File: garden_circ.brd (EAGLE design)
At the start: 89.8 x 83.8 mm, 39 parts, among them IC1 MEGA8-P, IC2 74HC595N, IC3 74HC595N, IC4 7805TV, J1 POWER_JACKSLT

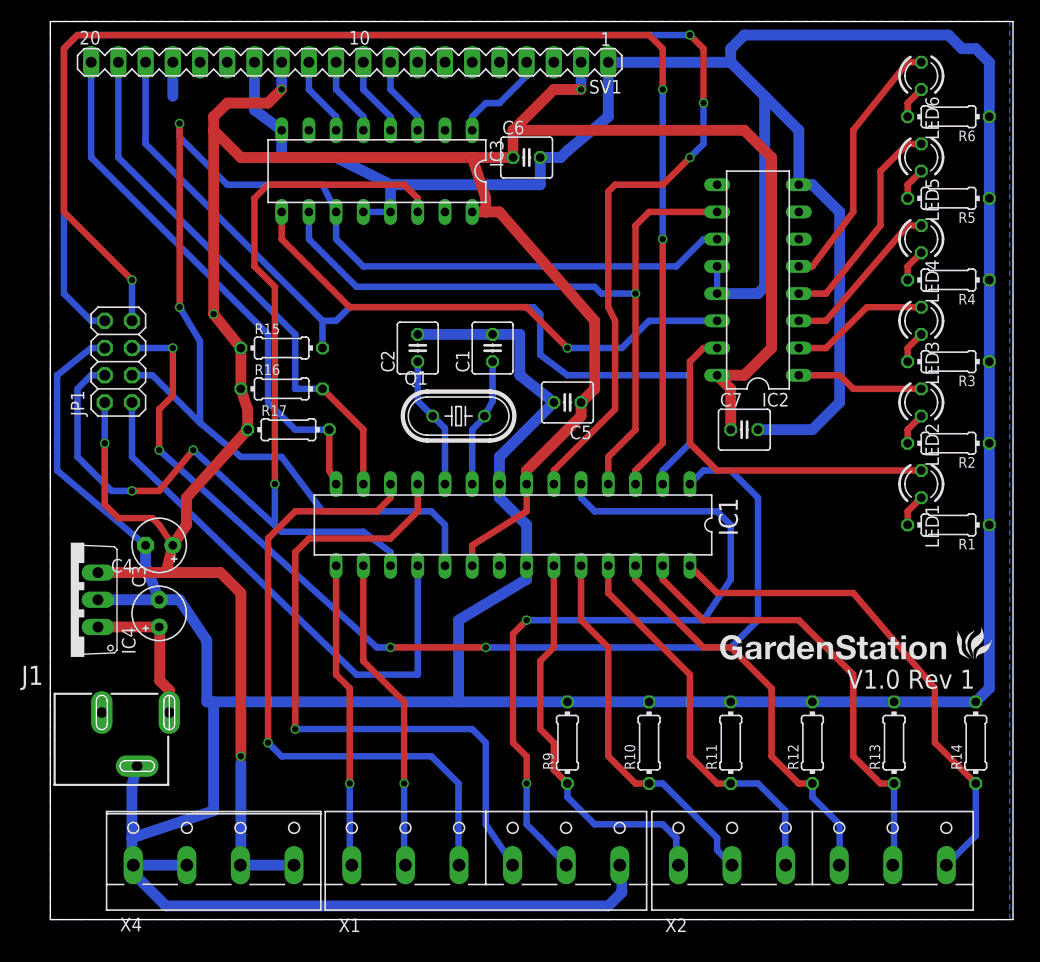
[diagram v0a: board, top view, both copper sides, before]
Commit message: Fixed shift register wiring
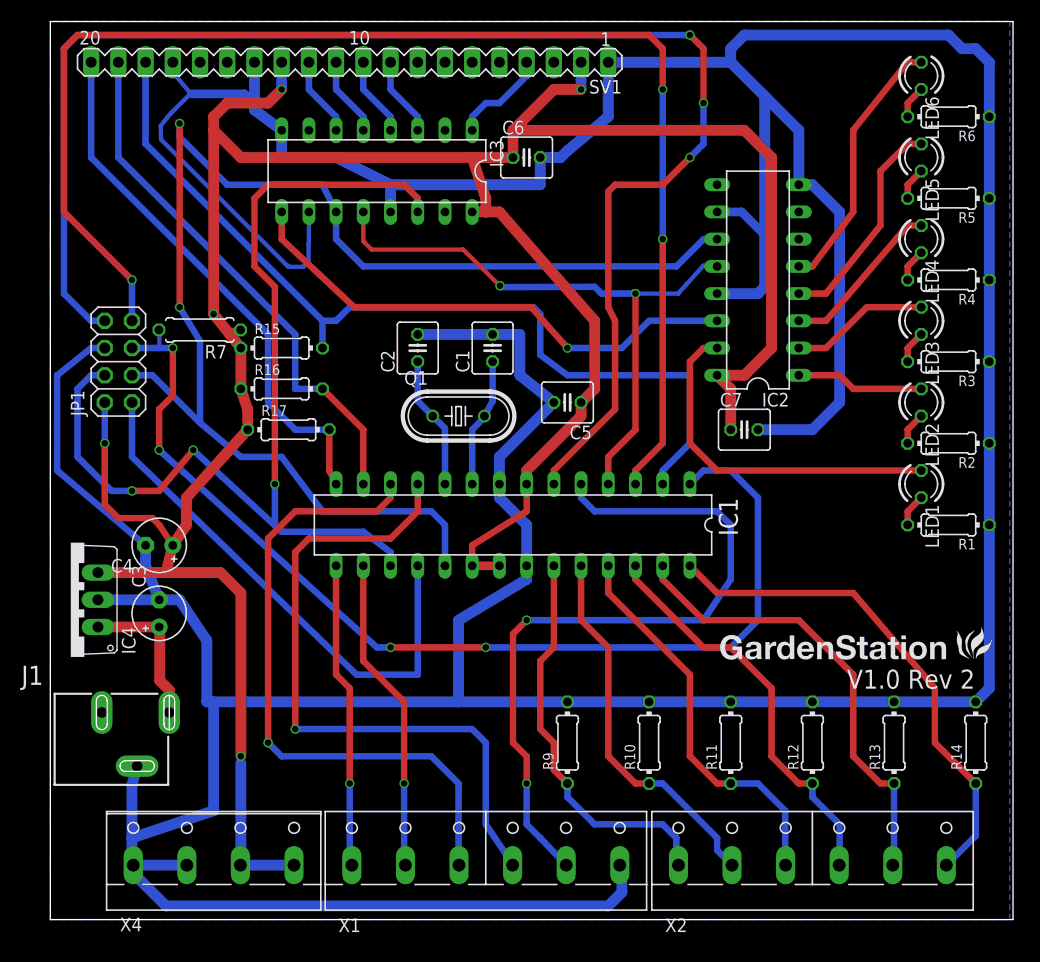
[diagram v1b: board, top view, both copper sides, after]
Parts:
- added R7: 10K, resistor:0207/7
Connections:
- removed net N$38: IC1.4, IC2.10, IC3.10
- new net N$52: IC1.4, IC2.12, IC3.12
- net GND: now also IC2.10, IC3.10; no longer IC2.12, IC3.12
- net N$10: now also R7.2
- net VCC: now also IC1.21, R7.1
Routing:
- net N$38: track 68.5 -> 0.00 mm
- net N$52: track 0.00 -> 58.2 mm, vias 0 -> 1
- net GND: track 483.2 -> 519.1 mm
- net VCC: track 264.7 -> 268.6 mm
- net N$10: track 97.3 -> 99.0 mm
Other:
- board text added: "V1.0 Rev 2"
- board text removed: "V1.0 Rev 1"

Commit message: Added code an SMD board
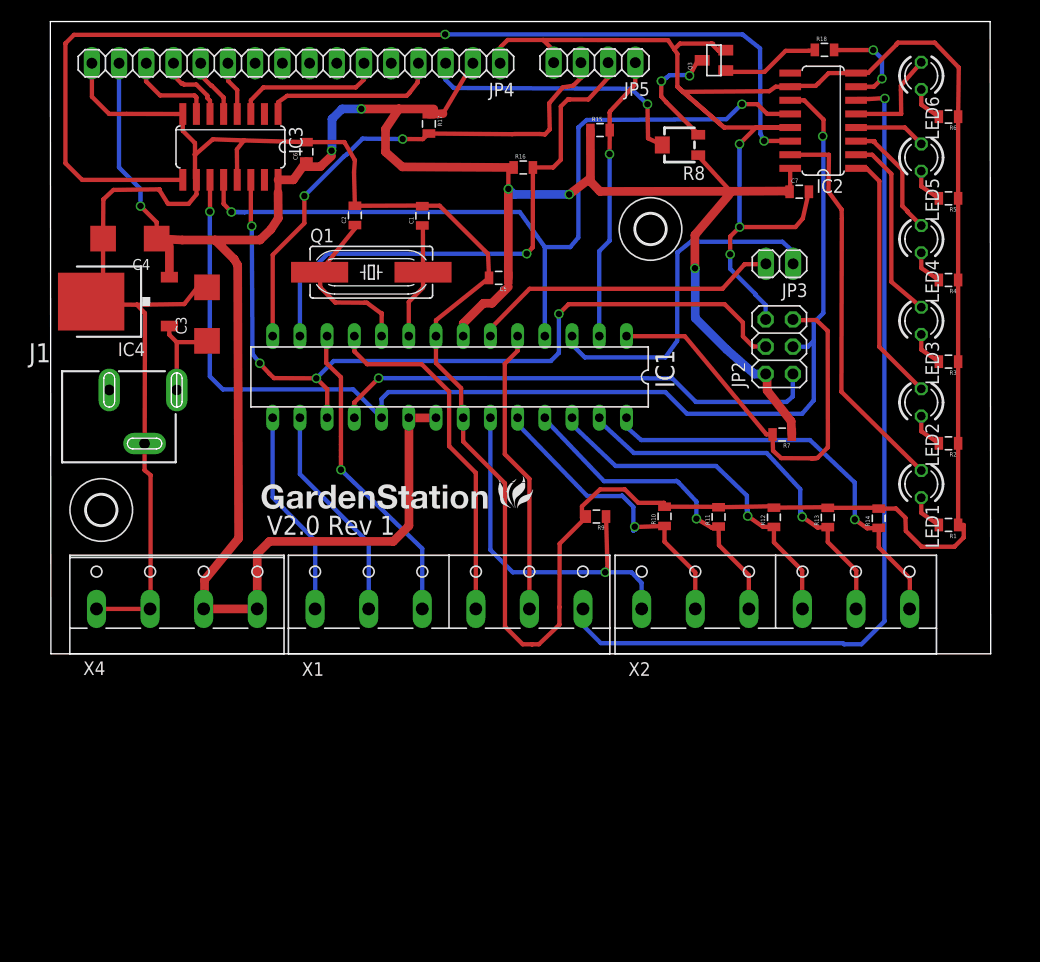
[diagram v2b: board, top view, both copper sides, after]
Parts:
- removed JP1: (no value), pinhead:2X04
- removed SV1: (no value), con-lstb:MA20-1
- added H1, H2: MOUNT-HOLE2.8, holes:2,8
- added JP2: (no value), pinhead:2X03
- added JP3: (no value), pinhead:1X02
- added JP4: (no value), pinhead:1X16
- added JP5: (no value), pinhead:1X04
- added Q3: MOSFET-NCHANNELBSS123LT1G, SparkFun-DiscreteSemi:SOT23
- added R18: (no value), SparkFun-Resistors:0805
- added R8: (no value), resistor:RTRIM3202
- C1, C2, C5, C6, C7: device rcl:C025-040X050 -> SparkFun-Capacitors:0805
- C3, C4: device resistor:E2,5-5 -> resistor:SMC_C
- IC2, IC3: value 74HC595N -> 74HC595D; device 74xx-eu:DIL16 -> 74xx-eu:SO16
- IC4: value 7805TV -> 7805DT; device linear:TO220V -> linear:TO252
- Q1: device crystal:HC49U-V -> crystal:HC49UP
- R1, R10, R11, R12, R13, R14, R15, R16, R17, R2, R3, R4, R5, R6, R9: device rcl:0204/7 -> SparkFun-Resistors:0805
- R7: device resistor:0207/7 -> SparkFun-Resistors:0805
- moved R7 55.2 mm to (64.5, 45.3)
- moved R15 36.0 mm to (47.5, 73.7)
- moved R17 31.4 mm to (31.5, 74.3), turned to 270 degrees
- moved R16 30.6 mm to (40.3, 70.2)
- moved J1 30.1 mm to (-5.81, 52.0)
- moved C4 28.8 mm to (3.61, 63.6)
- moved C3 28.3 mm to (10.8, 56.5)
- moved IC4 28.2 mm to (2.50, 57.7)
- moved X2 24.2 mm to (63.9, 30.3)
- moved X4 24.2 mm to (8.00, 30.3)
- moved X1 24.2 mm to (33.4, 30.3)
- moved R14 22.8 mm to (73.5, 37.5)
- moved C7 22.8 mm to (66.1, 67.9)
- moved R13 21.9 mm to (68.7, 37.5)
- moved R12 21.3 mm to (63.7, 37.5)
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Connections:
- new net MISO: IC1.18, JP2.1
- new net N$59: JP4.3, R8.2
- new net N$65: IC3.4, JP4.11
- new net N$66: Q3.3, R8.3
- new net N$67: IC2.7, R18.2
- new net N$68: Q3.1, R18.1
- net GND: now also IC4.3, JP2.6, JP4.1, JP4.16, JP5.4, Q3.2; no longer IC4.2, JP1.6, SV1.1, SV1.14, SV1.17, X1.6
- net N$10: now also JP2.5; no longer JP1.5
- net N$19: now also JP3.2; no longer JP1.8
- net N$20: now also JP2.3; no longer JP1.3
- net N$26: now also JP4.6; no longer SV1.9
- net N$27: now also JP4.4; no longer SV1.4
- net N$28: now also IC3.7, JP4.14; no longer IC3.4, SV1.10
- net N$29: now also IC3.6, JP4.13; no longer IC3.5, SV1.11
- net N$30: now also IC3.5, JP4.12; no longer IC3.6, SV1.12
- net N$39: now also JP5.1; no longer SV1.18
- net N$40: now also JP5.2; no longer SV1.19
- net N$41: now also JP5.3; no longer SV1.20
- net N$44: now also JP2.4; no longer JP1.4
- net N$45: now also JP3.1; no longer JP1.7
- net N$9: now also IC2.6, X1.6; no longer IC1.18, JP1.1
- net VCC: now also IC4.2, JP2.2, JP4.15, JP4.2, R8.1; no longer IC4.3, JP1.2, SV1.13, SV1.2
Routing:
- net GND: track 519.1 -> 376.9 mm, vias 0 -> 3
- net N$19: track 137.9 -> 29.0 mm, vias 3 -> 0
- net N$45: track 126.7 -> 33.1 mm, vias 3 -> 0
- net N$10: track 99.0 -> 40.4 mm, vias 4 -> 0
- net N$39: track 84.2 -> 26.9 mm, vias 0 -> 1
- net N$21: track 48.5 -> 99.6 mm, vias 1 -> 2
- net MISO: track 0.00 -> 46.5 mm, vias 0 -> 1
- net N$42: track 67.9 -> 26.9 mm, vias 2 -> 0
- net N$9: track 50.1 -> 83.0 mm, vias 0 -> 1
- net N$23: track 60.3 -> 29.3 mm
- net N$15: track 62.6 -> 33.1 mm, vias 1 -> 0
- net N$59: track 0.00 -> 26.0 mm, vias 0 -> 1
- net VCC: track 268.6 -> 243.9 mm, vias 5 -> 6
- net N$52: track 58.2 -> 78.7 mm, vias 1 -> 2
- net N$44: track 96.3 -> 76.7 mm, vias 3 -> 4
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- removed copper zone on layer 16, net GND
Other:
- board size 89.8 x 83.8 mm -> 87.8 x 59 mm
- board text added: "V2.0 Rev 1"
- board text removed: "V1.0 Rev 2"

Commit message: Added a few tweaks and power light
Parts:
- added H3, H4: MOUNT-HOLE2.8, holes:2,8
- added JP1: (no value), pinhead:1X04
- added LED7: (no value), led:SML0805
- added R19: 220, SparkFun-Resistors:0805
- added S1, S2, S3: SWITCH-MOMENTARY-2PTH, SparkFun-Electromechanical:TACTILE-PTH
- moved R18 68.2 mm to (0.94, 71.7)
- moved Q3 57.3 mm to (0.98, 75.6), turned to 0 degrees
- moved R14 0.38 mm to (73.6, 37.8)
- moved R10 0.32 mm to (53.5, 38.0)
- moved R12 0.28 mm to (63.7, 37.8)
- moved R13 0.28 mm to (68.7, 37.8)
- moved R11 0.24 mm to (58.6, 37.8)
- moved R9 0.11 mm to (47.3, 37.6)
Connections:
- new net N$69: IC3.2, R18.2
- new net N$70: JP1.2, S2.1
- new net N$71: JP1.3, S1.1
- new net N$72: JP1.4, S1.3, S2.3, S3.3
- new net N$73: LED7.C, R19.2
- net GND: now also JP4.5, R19.1, R8.3; no longer JP4.16
- net N$66: now also JP1.1, S3.1; no longer Q3.3, R8.3
- net N$67: now also JP4.16, Q3.3; no longer IC2.7, R18.2
- net VCC: now also LED7.A
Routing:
- net N$71: track 0.00 -> 37.8 mm
- net N$72: track 0.00 -> 36.1 mm
- net N$70: track 0.00 -> 26.1 mm
- net N$69: track 0.00 -> 16.7 mm, vias 0 -> 2
- net VCC: track 243.9 -> 251.9 mm
- net N$68: track 9.77 -> 3.00 mm
- net N$67: track 9.39 -> 3.56 mm, vias 2 -> 0
- net N$73: track 0.00 -> 5.12 mm
- net GND: track 376.9 -> 381.8 mm, vias 3 -> 4
- net N$66: track 11.3 -> 15.4 mm, vias 2 -> 0
- net N$33: track 33.7 -> 34.8 mm
- net N$34: track 36.4 -> 37.3 mm
- added copper zone on layer 1, net GND
- added copper zone on layer 16, net GND
- added copper zone on layer 1, net N$72
- added copper zone on layer 16, net N$72
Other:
- board size 87.8 x 59 mm -> 87.8 x 73.9 mm
